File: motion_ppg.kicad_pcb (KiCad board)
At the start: 2 copper layers, 32.2 x 20.5 mm, 62 parts, among them IC1 SFH_7070, P1 CONN_2, P2 CONN_2, P3 CONN_2, Q1 DMP21D5UFB4-7B, U1 TPS63001, U2 TPS62746, U3 NRF528XX-QFAA, U4 ICM-20948, U5 MCP6001-OT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

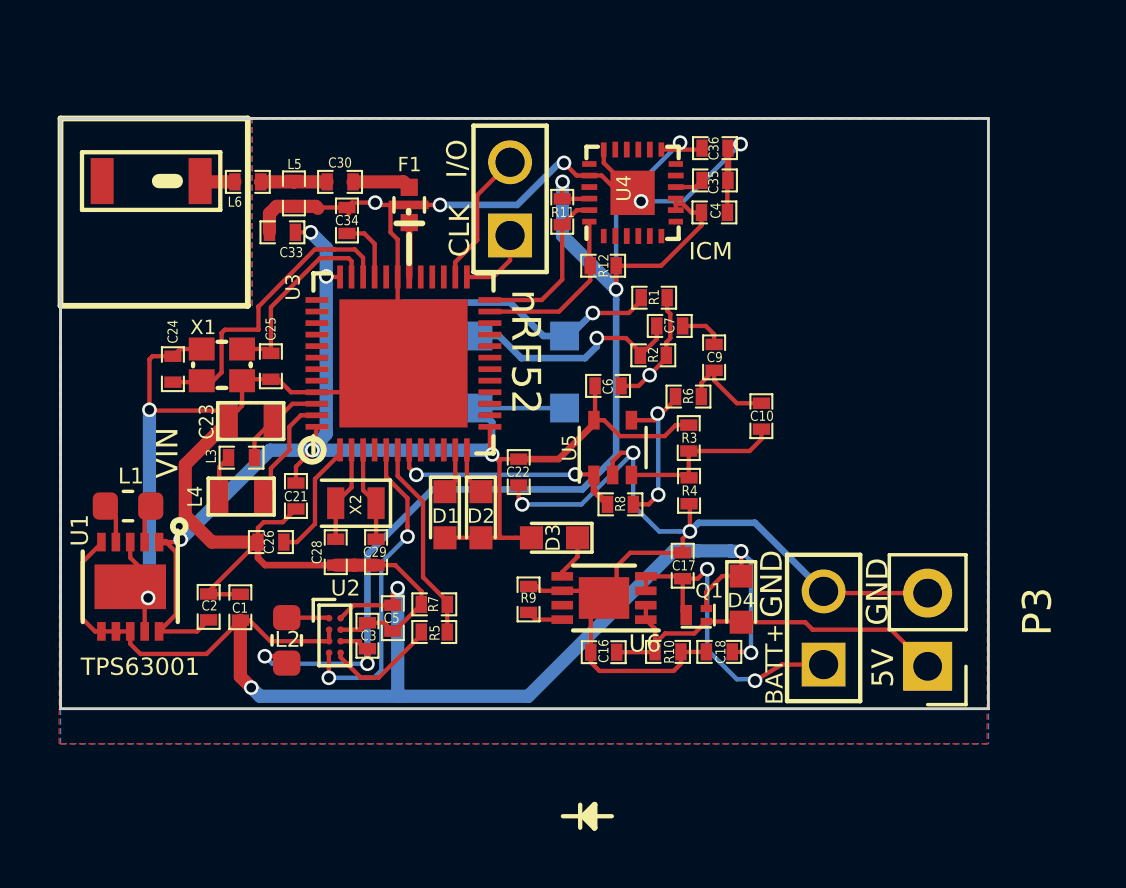
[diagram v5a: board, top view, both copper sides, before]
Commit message: Changed footprint for MCP6001 from SC-70-5 to SOT-23-5.
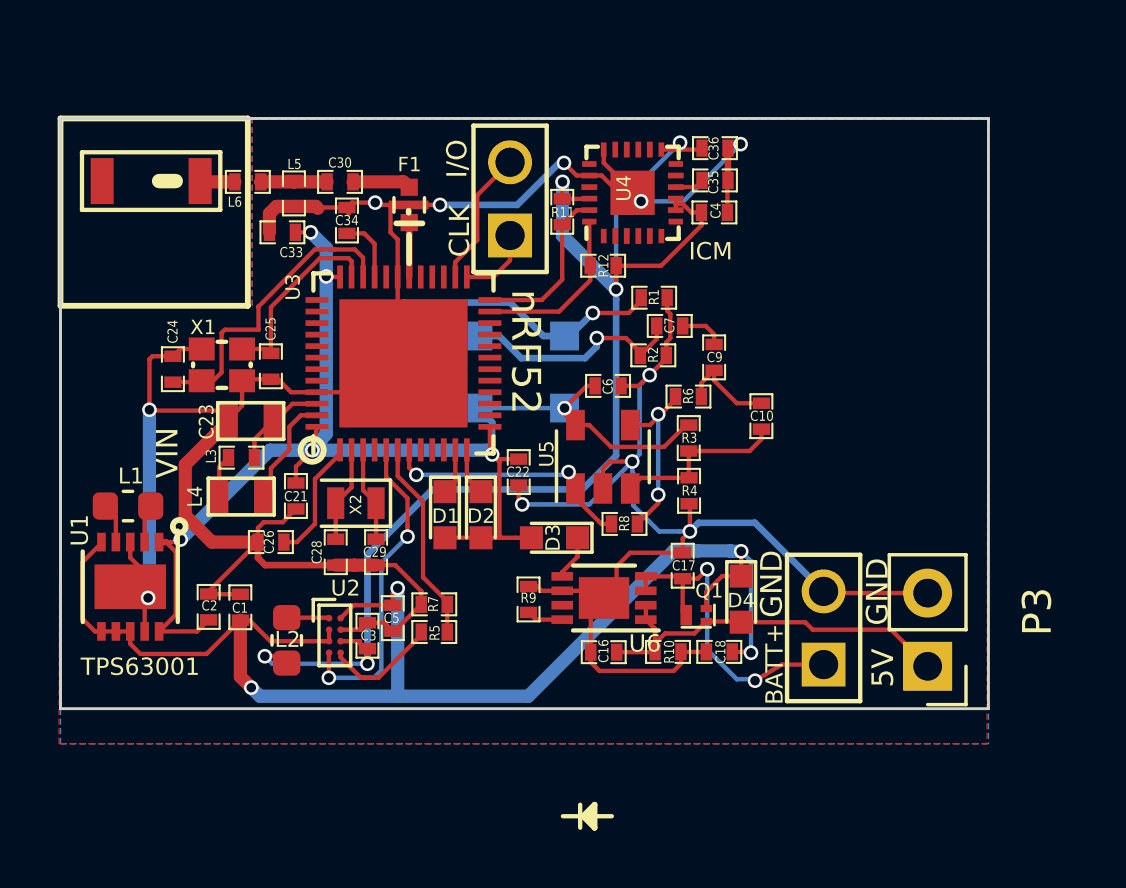
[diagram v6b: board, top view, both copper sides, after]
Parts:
- U5: footprint Package_TO_SOT_SMD:SOT-353_SC-70-5 -> Package_TO_SOT_SMD:SOT-23-5
- moved R8 0.69 mm to (285.5, 139.6)
- moved U5 0.47 mm to (284.7, 137.2)
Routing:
- net DGND: track 133.4 -> 136.7 mm
- net DVDD: track 53.7 -> 52.5 mm, vias 5 -> 6
- net Net-(R6-Pad2): track 5.75 -> 6.37 mm
- net /ppg_amp_out: track 8.36 -> 8.91 mm
